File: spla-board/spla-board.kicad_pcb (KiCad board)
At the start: 4 copper layers, 178 x 107 mm, 272 parts, among them J1 USB_B_Micro, J12 J_POWER, J13 J_ANALOG, J14 J_AREF, J15 J_DPULL, J2 J_JTAG, J3 J_BODGE, J4 J_POWER2, J5 J_PPURESET, J6 J_SAMPLE, J7 Barrel_Jack, J8 J_AREF_AMP, U1 LFE5U-45F-BG256, U10 SNES_PPU1, U11 SNES_PPU2, U12 VRAM, U13 VRAM, U14 TLV73311PDBV, U15 74LVC8T245, U16 74LVC8T245, U17 74LVC8T245, U2 FT2232H, U20 74LVC8T245, U22 74LVC8T245, U23 74LVC8T245, U24 74LVC8T245, U25 74LVC8T245, U26 74LVC8T245, U27 74LVC8T245, U28 74LVC8T245, U29 74LVC8T245, U3 93LC66B, U30 74LVC8T245, U31 74LVC8T245, U32 74LVC8T245, U51 ADC1173, U52 ADC1173, U53 ADC1173, U61 LMH6611, U62 LMH6611, U63 LMH6611, U7 ST1S10PHR, U74 LMH6611, U75 LMH6611, U76 TLV73333PDBV, U8 ST1S10PHR, U9 TLV73325PDBV, X1 FT5HNBPK12.0-T1

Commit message: pcb: Export revision 9.
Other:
- board text added: "SPLA Breakout Board Rev 009 Batch 1 2020-04-26"
- board text removed: "SPLA Breakout Board Rev 009 Batch 1 2020-04-24"
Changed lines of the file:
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@@
   )
   (page A4)
+  (title_block
+    (date 2020-04-26)
+    (rev 9)
+  )
   (layers
     (0 F.Cu signal)
@@
   )
   (setup
-    (last_trace_width 0.4)
+    (last_trace_width 0.1)
     (user_trace_width 0.1)
     (user_trace_width 0.2)
@@
       (usegerberadvancedattributes false)
       (creategerberjobfile false)
-      (excludeedgelayer true)
+      (excludeedgelayer false)
       (linewidth 0.100000)
       (plotframeref false)
@@
       (padsonsilk false)
       (subtractmaskfromsilk false)
-      (outputformat 4)
+      (outputformat 1)
       (mirror false)
       (drillshape 0)
       (scaleselection 1)
-      (outputdirectory "../"))
+      (outputdirectory "./gerber"))
   )
   (net 0 "")
@@
     )
   )
-  (gr_text "SPLA Breakout Board\nRev 009 Batch 1\n2020-04-24" (at 180 55) (layer F.SilkS)
+  (gr_text "SPLA Breakout Board\nRev 009 Batch 1\n2020-04-26" (at 180 55) (layer F.SilkS)
     (effects (font (size 1.5 1.5) (thickness 0.2)) (justify left))
   )

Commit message: schematic/pcb: Update for new KiCad version; no meaningfuly changes.
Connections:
- net LED4 renamed LED7
- net LED6 renamed LED8

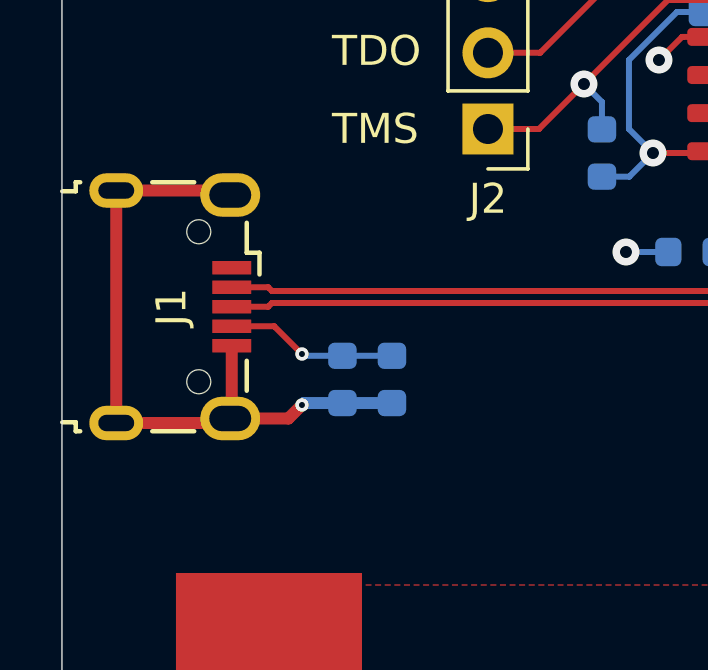
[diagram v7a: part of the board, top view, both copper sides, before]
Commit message: schematic/pcb: Disconnect USB shield from ground.
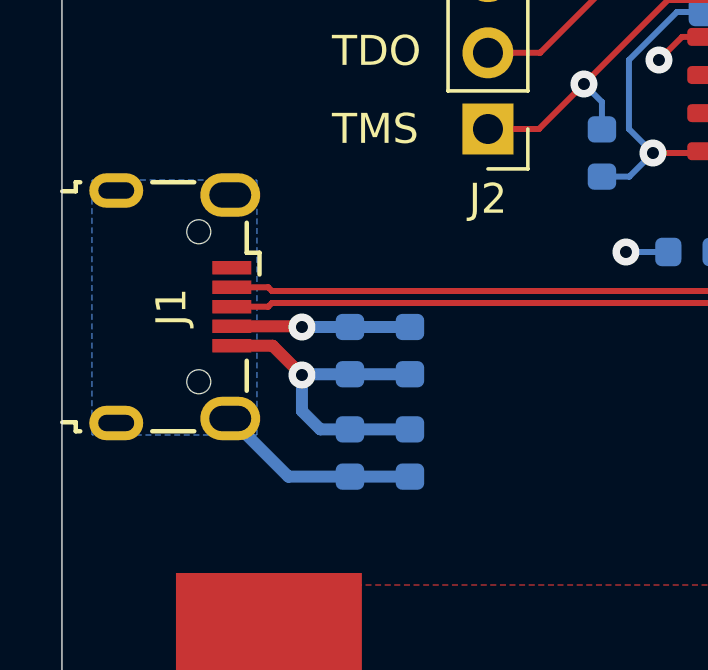
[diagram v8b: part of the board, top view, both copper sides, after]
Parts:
- added C44: 0.1uF, Capacitor_SMD:C_0603_1608Metric, B.Cu at (51.6, 120.6)
- added R32: 0, Resistor_SMD:R_0603_1608Metric, B.Cu at (49.6, 120.6)
- moved R1 1.13 mm to (51.6, 117.2)
- moved C1 0.99 mm to (49.6, 117.2)
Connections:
- net Net-(J1-Pad1) renamed /SPLA Board - USB/VBUS
- J1 pad 6: GND -> /SPLA Board - USB/SHIELD
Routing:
- net GND: track 469.6 -> 457.4 mm
- net /SPLA Board - USB/SHIELD: track 0.00 -> 6.80 mm
- added copper zone on B.Cu, net /SPLA Board - USB/SHIELD
